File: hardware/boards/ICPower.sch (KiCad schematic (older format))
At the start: 22 parts, among them U1 ECP5UM5G-381caBGA, U3 CYUSB3014, U4 IS43TR16256B-125KBL, U5 128MiB

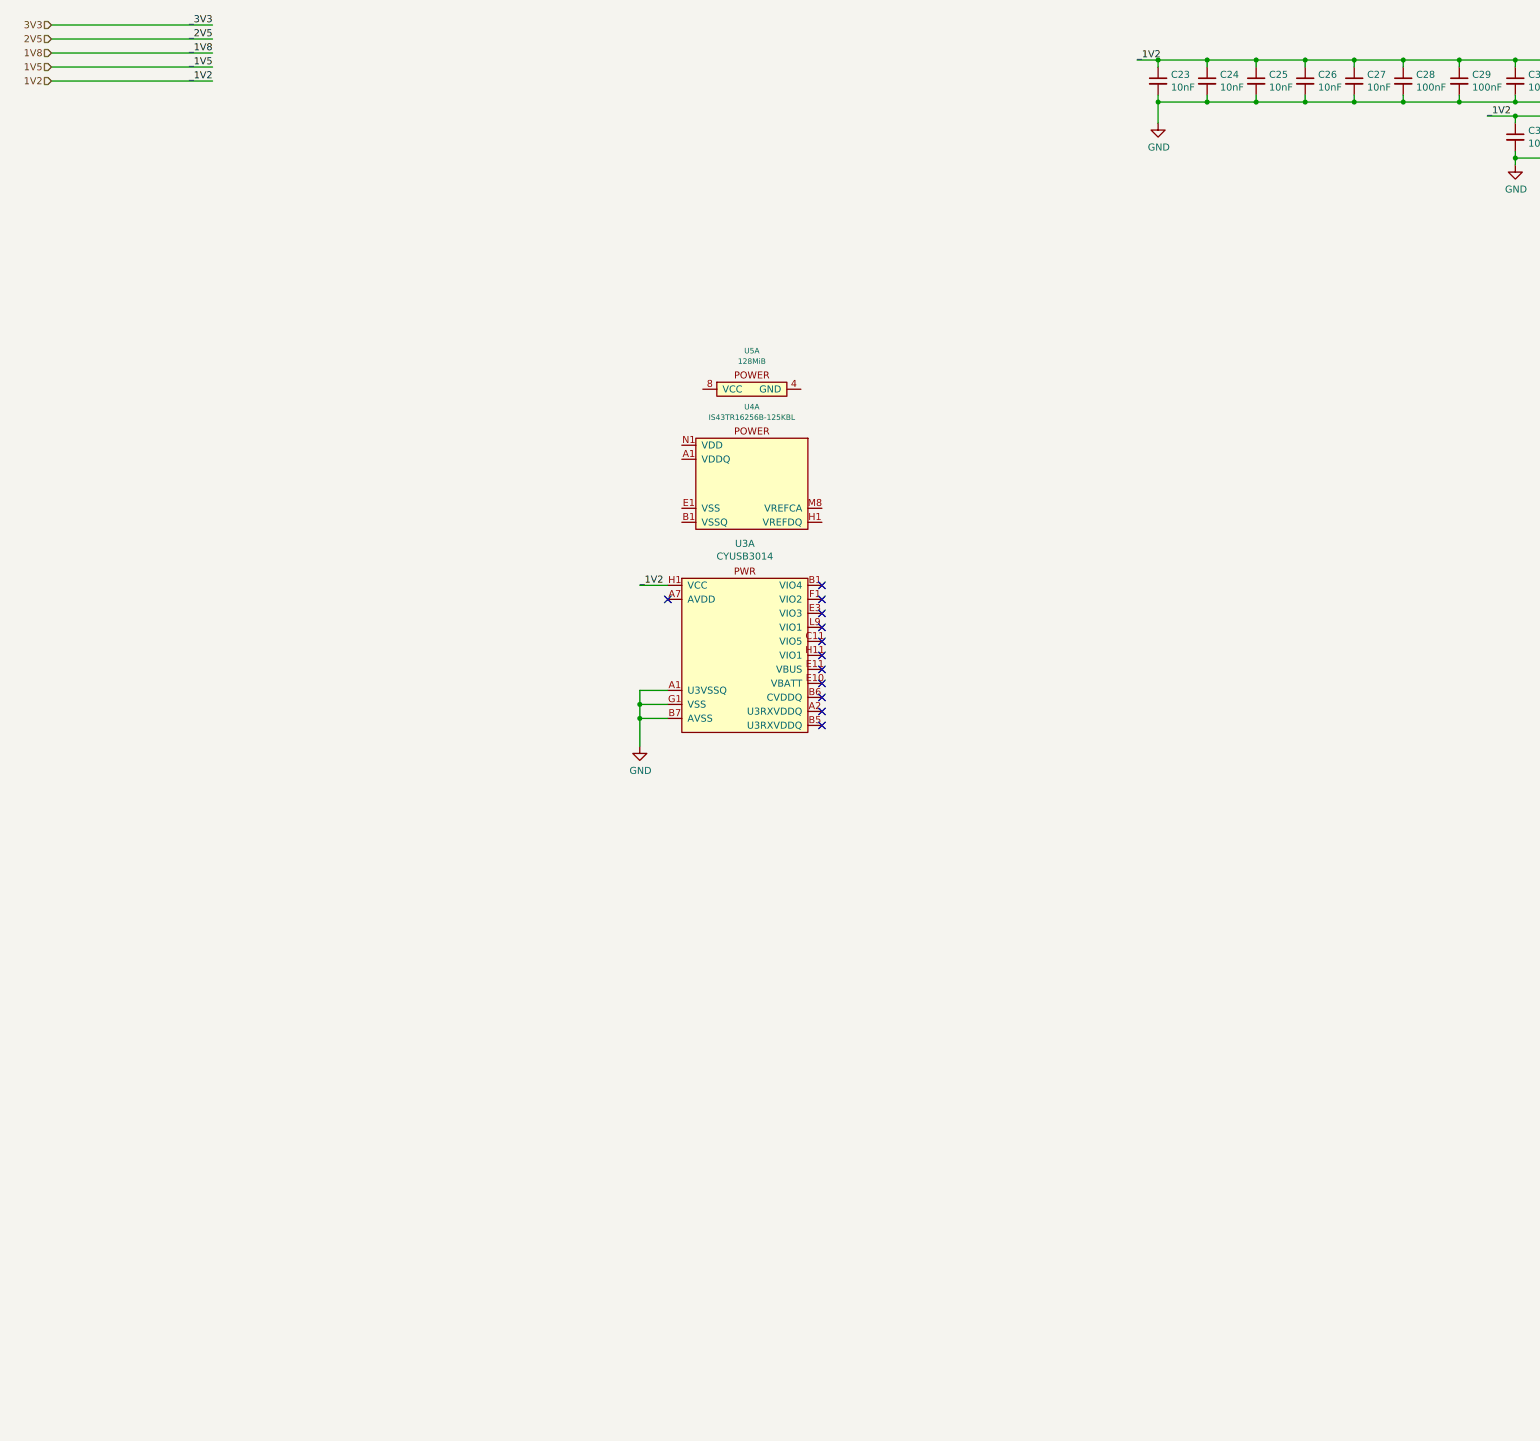
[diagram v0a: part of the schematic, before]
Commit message: In an AHDH fuled stupor I made a bunch of changes, only the last of which I recall, which would be adding fiducials
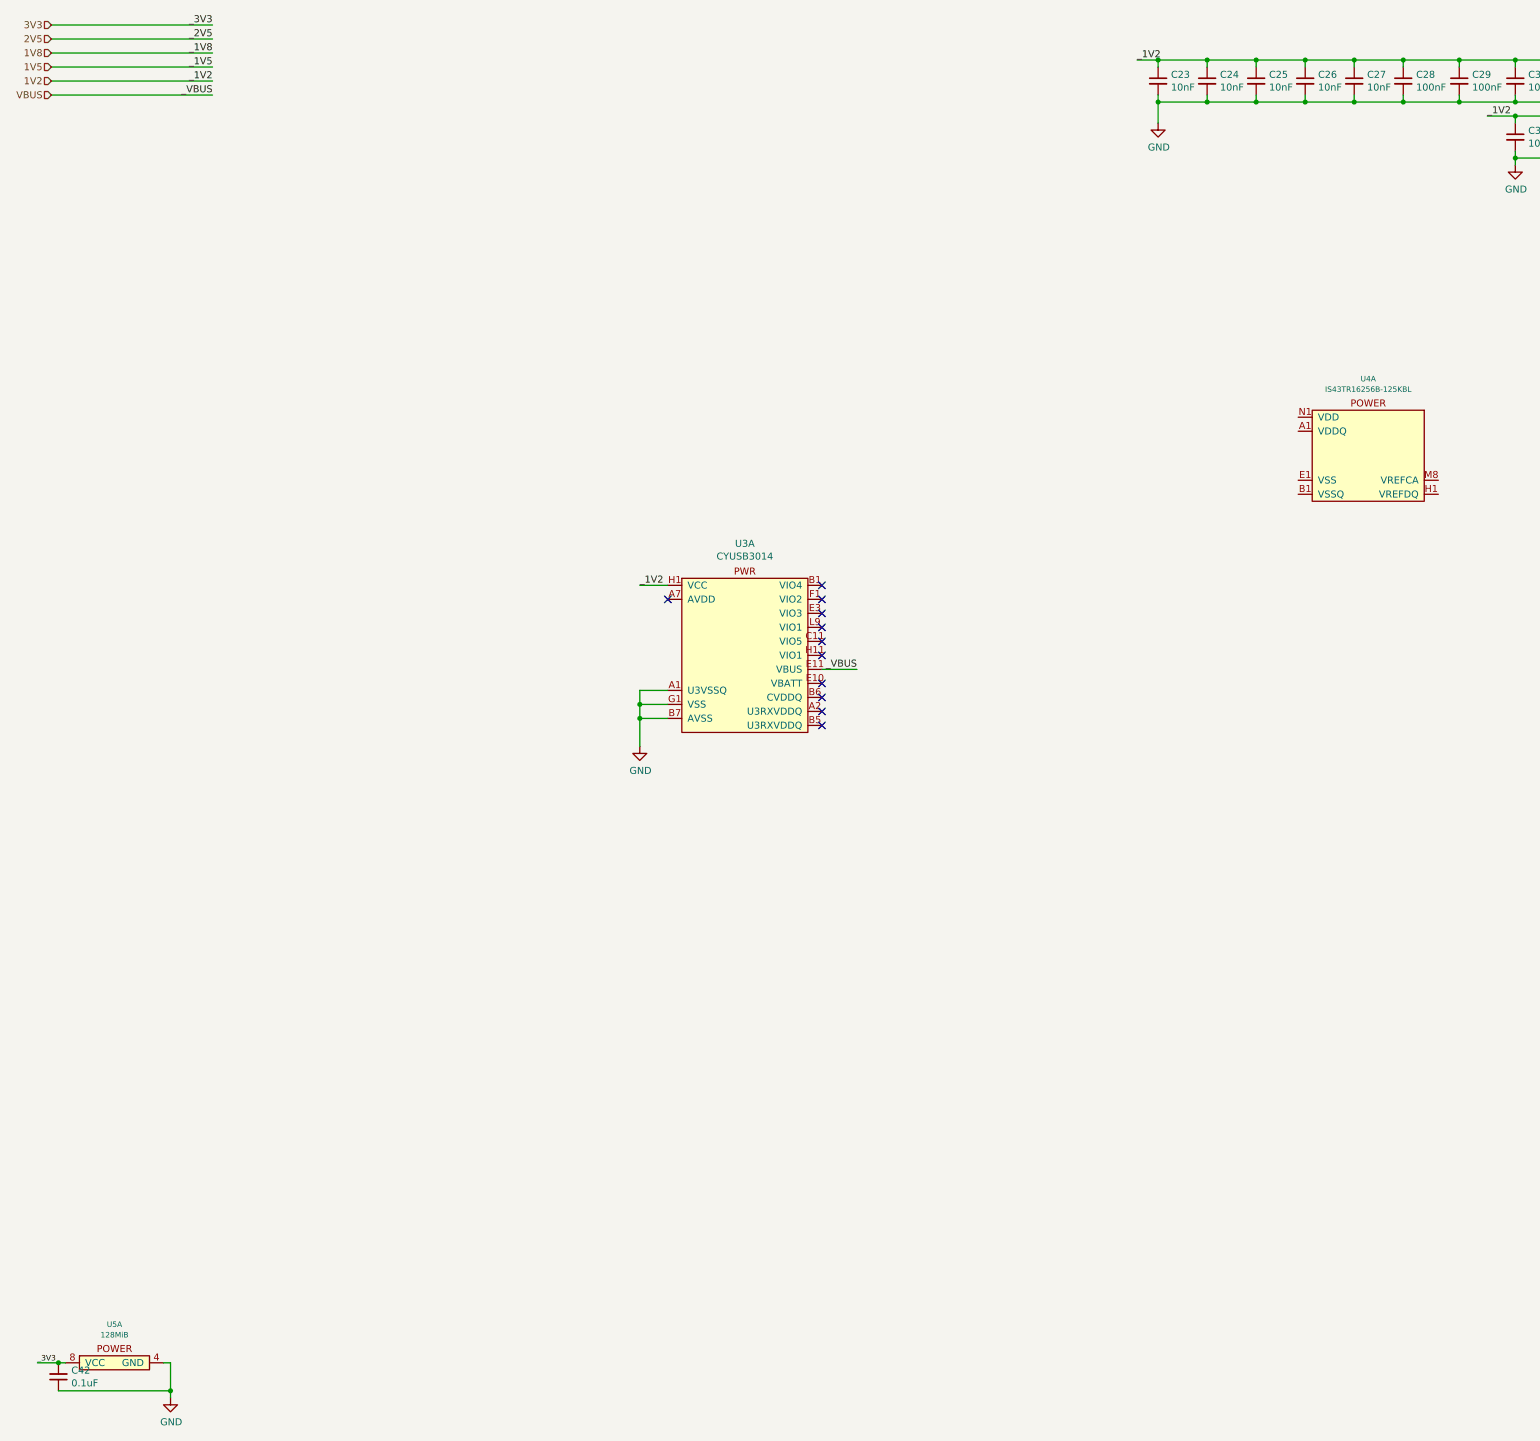
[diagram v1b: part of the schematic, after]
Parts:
- added C42: 0.1uF, Capacitor_SMD:C_0603_1608Metric, symbol Device:C_Small
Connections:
- net 3V3: now also U5.8 (VCC), C42.2
- net GND: now also U5.4 (GND), U5.9 (GND), C42.1
- net VBUS: now reaches U3.E11 (VBUS)
- no-connect marks 20 -> 19
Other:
- moved on the sheet: U4A, U5A
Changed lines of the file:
@@
 NoConn ~ 6300 5100
 NoConn ~ 6300 5200
-NoConn ~ 6300 5300
 NoConn ~ 6300 5400
 NoConn ~ 6300 5500
@@
 L lethalbit-memory:IS43TR16256B-125KBL U4
 U 1 1 5F1E5A2E
-P 5800 3900
-F 0 "U4" H 5800 4374 39  0000 C CNN
-F 1 "IS43TR16256B-125KBL" H 5800 4299 39  0000 C CNN
-F 2 "Package_BGA:BGA-96_9.0x13.0mm_Layout2x3x16_P0.8mm" H 5800 4300 39  0001 C CNN
-F 3 "http://www.issi.com/WW/pdf/43-46TR16256B-85120BL.pdf" H 5800 4300 39  0001 C CNN
-F 4 "ISSI" H 5800 3900 50  0001 C CNN "MFR"
-F 5 "IS43TR16256B-125KBL" H 5800 3900 50  0001 C CNN "MPN"
-	1    5800 3900
+P 10200 3700
+F 0 "U4" H 10200 4174 39  0000 C CNN
+F 1 "IS43TR16256B-125KBL" H 10200 4099 39  0000 C CNN
+F 2 "Package_BGA:BGA-96_9.0x13.0mm_Layout2x3x16_P0.8mm" H 10200 4100 39  0001 C CNN
+F 3 "http://www.issi.com/WW/pdf/43-46TR16256B-85120BL.pdf" H 10200 4100 39  0001 C CNN
+F 4 "ISSI" H 10200 3700 50  0001 C CNN "MFR"
+F 5 "IS43TR16256B-125KBL" H 10200 3700 50  0001 C CNN "MPN"
+	1    10200 3700
 	1    0    0    -1
 $EndComp
@@
 L lethalbit-memory:W25N01GVZEIG U5
 U 1 1 5F208622
-P 5800 3250
-F 0 "U5" H 5800 3474 39  0000 C CNN
-F 1 "128MiB" H 5800 3399 39  0000 C CNN
-F 2 "lethalbit-memory:WSON-8-1EP-6.0x8.0mm" H 5800 3400 39  0001 C CNN
-F 3 "https://www.winbond.com/resource-files/w25n01gv%20revl%20050918%20unsecured.pdf" H 5800 3400 39  0001 C CNN
-F 4 "Winbond" H 5800 3250 50  0001 C CNN "MFR"
-F 5 "W25N01GVZEIG TR" H 5800 3250 50  0001 C CNN "MPN"
-	1    5800 3250
+P 1250 10200
+F 0 "U5" H 1250 10424 39  0000 C CNN
+F 1 "128MiB" H 1250 10349 39  0000 C CNN
+F 2 "lethalbit-memory:WSON-8-1EP-6.0x8.0mm" H 1250 10350 39  0001 C CNN
+F 3 "https://www.winbond.com/resource-files/w25n01gv%20revl%20050918%20unsecured.pdf" H 1250 10350 39  0001 C CNN
+F 4 "Winbond" H 1250 10200 50  0001 C CNN "MFR"
+F 5 "W25N01GVZEIG TR" H 1250 10200 50  0001 C CNN "MPN"
+	1    1250 10200
 	1    0    0    -1
 $EndComp
+Wire Wire Line
+	850  10250 700  10250
+Text Label 700  10250 0    39   ~ 0
+_3V3
+$Comp
+L power:GND #PWR0122
+U 1 1 5F6C47FF
+P 1650 10500
+F 0 "#PWR0122" H 1650 10250 50  0001 C CNN
+F 1 "GND" H 1655 10327 50  0000 C CNN
+F 2 "" H 1650 10500 50  0001 C CNN
+F 3 "" H 1650 10500 50  0001 C CNN
+	1    1650 10500
+	1    0    0    -1
+$EndComp
+Wire Wire Line
+	1600 10250 1650 10250
+Wire Wire Line
+	1650 10250 1650 10450
+$Comp
+L Device:C_Small C?
+U 1 1 5F7157B7
+P 850 10350
+AR Path="/5EDF9F51/5F7157B7" Ref="C?"  Part="1"
+AR Path="/5EF66188/5F7157B7" Ref="C42"  Part="1"
+F 0 "C42" H 758 10304 50  0000 R CNN
+F 1 "0.1uF" H 758 10395 50  0000 R CNN
+F 2 "Capacitor_SMD:C_0603_1608Metric" H 850 10350 50  0001 C CNN
+F 3 "~" H 850 10350 50  0001 C CNN
+F 4 "KEMET" V 850 10350 50  0001 C CNN "MFR"
+F 5 "C0603C104M5RACTU" V 850 10350 50  0001 C CNN "MPN"
+	1    850  10350
+	-1   0    0    1
+$EndComp
+Wire Wire Line
+	850  10250 900  10250
+Connection ~ 850  10250
+Wire Wire Line
+	850  10450 1650 10450
+Connection ~ 1650 10450
+Wire Wire Line
+	1650 10450 1650 10500
+Text HLabel 800  1200 0    50   Input ~ 0
+VBUS
+Wire Wire Line
+	800  1200 1950 1200
+Text Label 1950 1200 2    50   ~ 0
+_VBUS
+Wire Wire Line
+	6300 5300 6550 5300
+Text Label 6550 5300 2    50   ~ 0
+_VBUS
 $EndSCHEMATC

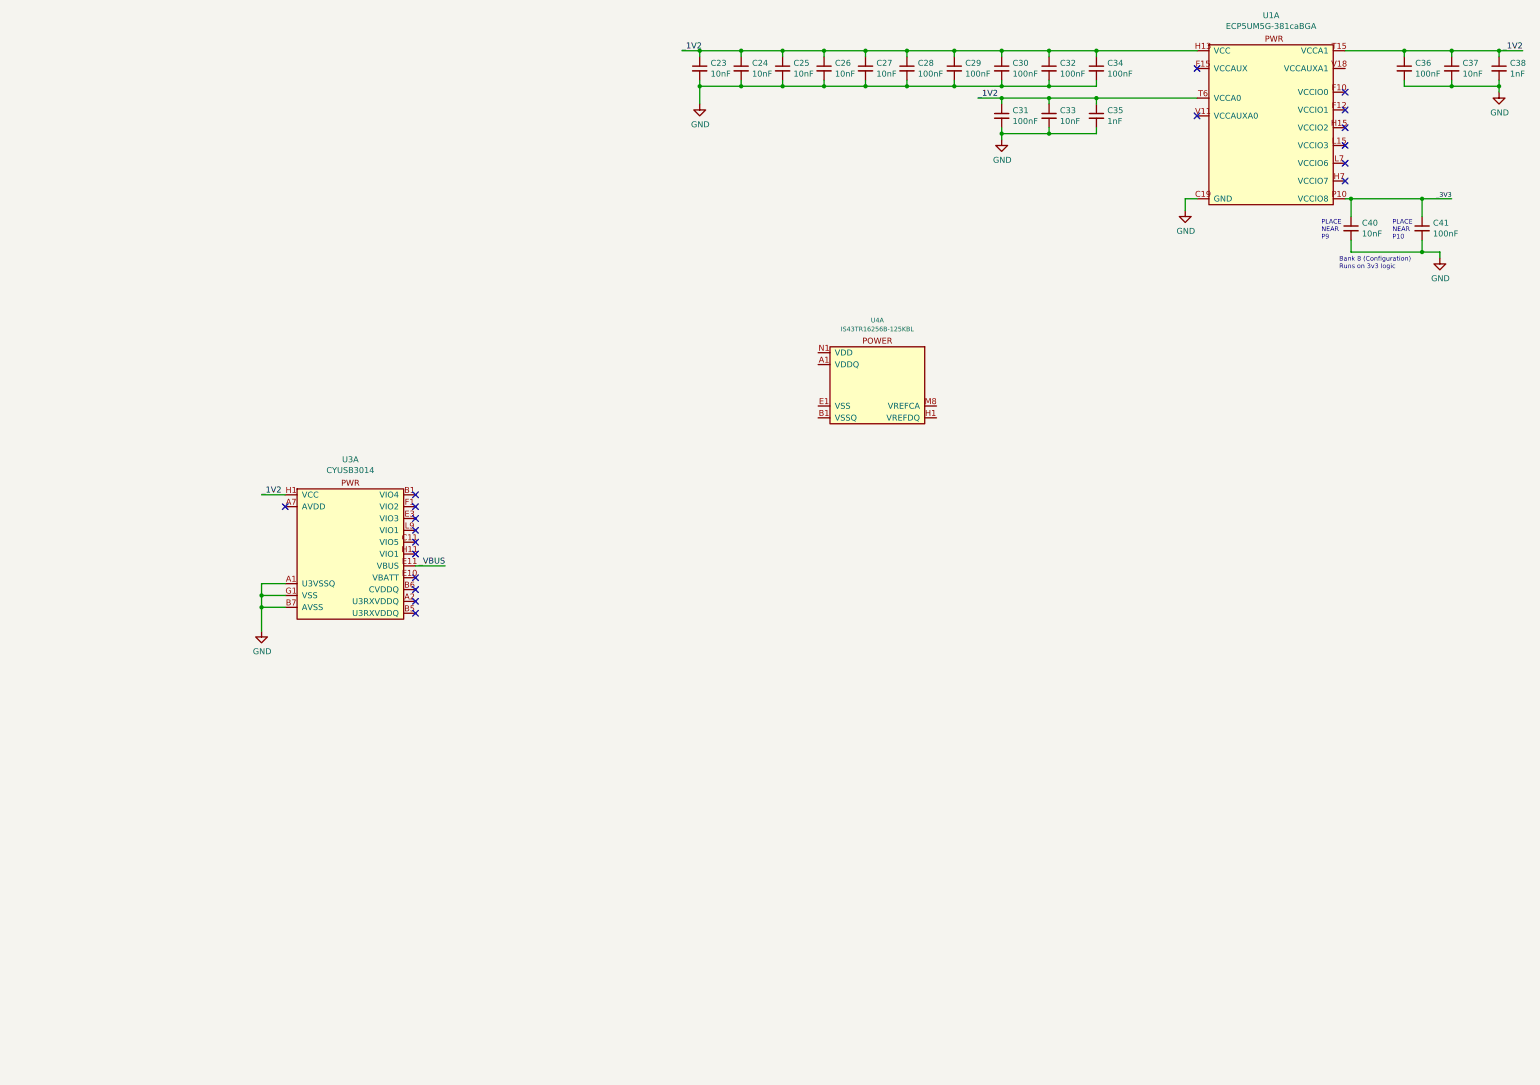
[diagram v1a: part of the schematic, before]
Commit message: Worked on a bit of the power side for the DDR3 Cache
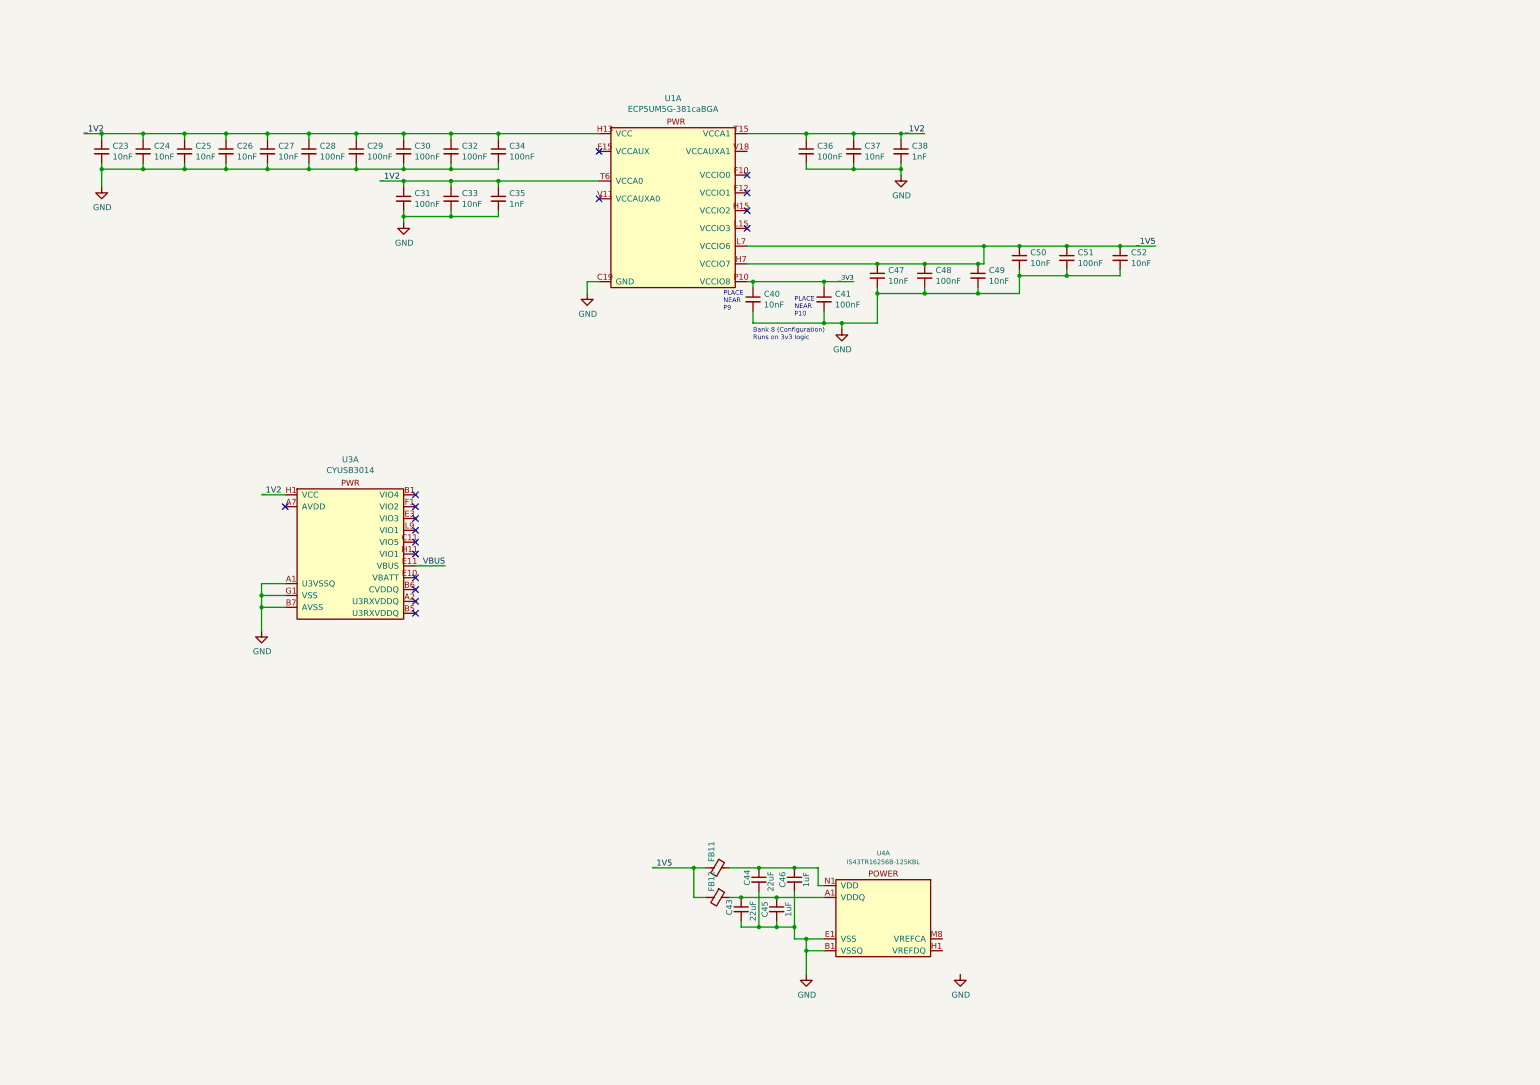
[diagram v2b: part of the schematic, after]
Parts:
- added C43, C44: 22uF, Capacitor_SMD:C_1206_3216Metric, symbol Device:C_Small
- added C45, C46: 1uF, Capacitor_SMD:C_0603_1608Metric, symbol Device:C_Small
- added C47, C49, C50, C52: 10nF, Capacitor_SMD:C_0402_1005Metric, symbol Device:C_Small
- added C48, C51: 100nF, Capacitor_SMD:C_0402_1005Metric, symbol Device:C_Small
- added FB11, FB12: 220 @ 100Mhz, Resistor_SMD:R_0603_1608Metric, symbol Device:Ferrite_Bead_Small
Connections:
- net 1V5: now also U1.H6 (VCCIO7), U1.H7 (VCCIO7), U1.J6 (VCCIO7), U1.L6 (VCCIO6), U1.L7 (VCCIO6), U1.M6 (VCCIO6), C47.1, C48.1, C49.1, C50.1, C51.1, C52.1, FB11.2, FB12.2
- net GND: now also U4.A9 (VSS), U4.B1 (VSSQ), U4.B3 (VSS), U4.B9 (VSSQ), U4.D1 (VSSQ), U4.D8 (VSSQ), U4.E1 (VSS), U4.E2 (VSSQ), U4.E8 (VSSQ), U4.F9 (VSSQ), U4.G1 (VSSQ), U4.G8 (VSS), U4.G9 (VSSQ), U4.J2 (VSS), U4.J8 (VSS), U4.M1 (VSS), U4.M9 (VSS), U4.P1 (VSS), U4.P9 (VSS), U4.T1 (VSS), U4.T9 (VSS), C43.2, C44.2, C45.2, C46.2, C47.2, C48.2, C49.2, C50.2, C51.2, C52.2
- net at U4.A1 (VDDQ), U4.A8 (VDDQ), U4.C1 (VDDQ)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: now also C43.1, C45.1, FB12.1
- net at U4.B2 (VDD), U4.D9 (VDD), U4.G7 (VDD)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: now also C44.1, C46.1, FB11.1
- no-connect marks 19 -> 17
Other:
- moved on the sheet: C23, C24, C25, C26, C27, C28, C29, C30, C31, C32, C33, C34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

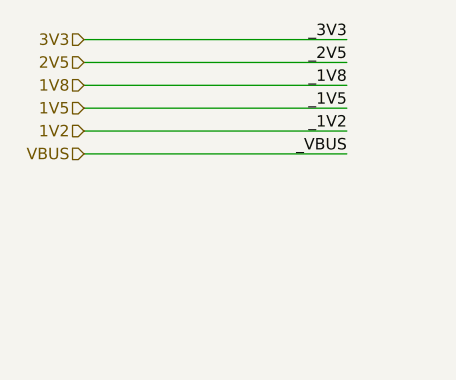
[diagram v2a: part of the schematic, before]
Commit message: Added the JTAG header and some misc cleanup
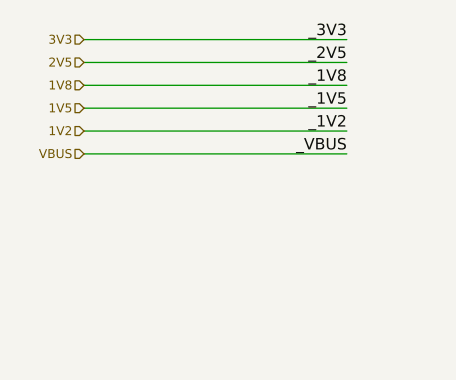
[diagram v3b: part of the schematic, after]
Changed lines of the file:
@@
 $Descr A3 16535 11693
 encoding utf-8
-Sheet 7 11
+Sheet 6 11
 Title "lethallink - IC Power Distribution"
 Date "2020-06-13"
@@
 Wire Wire Line
 	9600 1650 10000 1650
-Text HLabel 800  700  0    50   Input ~ 0
+Text HLabel 800  700  0    39   Input ~ 0
 3V3
-Text HLabel 800  1000 0    50   Input ~ 0
+Text HLabel 800  1000 0    39   Input ~ 0
 1V5
-Text HLabel 800  900  0    50   Input ~ 0
+Text HLabel 800  900  0    39   Input ~ 0
 1V8
-Text HLabel 800  800  0    50   Input ~ 0
+Text HLabel 800  800  0    39   Input ~ 0
 2V5
-Text HLabel 800  1100 0    50   Input ~ 0
+Text HLabel 800  1100 0    39   Input ~ 0
 1V2
 Wire Wire Line
@@
 Wire Wire Line
 	1650 10450 1650 10500
-Text HLabel 800  1200 0    50   Input ~ 0
+Text HLabel 800  1200 0    39   Input ~ 0
 VBUS
 Wire Wire Line
